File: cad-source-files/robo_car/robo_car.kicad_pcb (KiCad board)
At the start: 2 copper layers, 100 x 100 mm, 87 parts, among them J1 Conn_01x06_MountingPin, J16 Conn_01x02_MountingPin, J2 ftdi_conn, J3 Conn_01x06_MountingPin, J4 Conn_01x04, J5 Conn_01x04, J6 Conn_01x06_MountingPin, J7 Conn_01x02_MountingPin, J8 Conn_01x02_MountingPin, SW1 SW_Push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

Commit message: move Olivia's stuffy stuff to the correct repo
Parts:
- removed D7: D_TVS_x2_AAC, Package_TO_SOT_SMD:SOT-23
- removed U5: Trans_CAN_SN65HVD230DR, Package_SO:CAN-TRANS-SN65HVD230DR
- added C14: 22uF, Capacitor_SMD:C_0805_2012Metric, F.Cu at (175.7, 147.5)
- added C16: 22uF, Capacitor_SMD:C_0805_2012Metric, F.Cu at (179.4, 126.5)
- added H28: MountingHole, MountingHole:MountingHole_3.2mm_M3_ISO14580, F.Cu at (190.0, 111.0)
- added H29: MountingHole, MountingHole:MountingHole_3.2mm_M3_ISO14580, F.Cu at (110.0, 111.0)
- J2: footprint Connector_JST:JST_SH_BM06B-SRSS-TB_1x06-1MP_P1.00mm_Vertical -> Connector_JST:JST_SH_SM06B-SRSS-TB_1x06-1MP_P1.00mm_Horizontal
- J4: value Conn_01x04 -> Barrel_Jack; footprint Connector_JST:JST_PH_B4B-PH-SM4-TB_1x04-1MP_P2.00mm_Vertical -> Connector_BarrelJack:BarrelJack_Horizontal
- J5: footprint Connector_JST:JST_PH_S4B-PH-SM4-TB_1x04-1MP_P2.00mm_Horizontal -> Connector_PinSocket_2.54mm:PinSocket_1x04_P2.54mm_Vertical
- moved C9 45.6 mm to (181.6, 141.7), turned to 180 degrees
- moved C15 41.3 mm to (179.5, 123.7), turned to 0 degrees
- moved J5 14.8 mm to (146.9, 144.7), turned to -90 degrees
- moved J2 13.2 mm to (129.6, 146.7), turned to 0 degrees
- moved J4 6.18 mm to (118.4, 136.2)
- moved R3 4.47 mm to (185.7, 110.2)
- moved R6 3.52 mm to (181.7, 143.8)
- moved C7 3.49 mm to (178.0, 144.7), turned to 90 degrees
- moved U2 1.50 mm to (180.8, 135.9)
- moved H14 1.00 mm to (110.0, 146.0)
- moved H19 1.00 mm to (190.0, 146.0)
- moved H21 1.00 mm to (110.0, 120.0)
- moved H22 1.00 mm to (190.0, 120.0)
- moved H23 1.00 mm to (190.0, 138.0)
- moved H24 1.00 mm to (110.0, 138.0)
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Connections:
- C15 pad 1: +3V3 -> /VREG_OUT
- J4 pad 1: /CAN_H -> VBUS
- J4 pad 2: /CAN_L -> GND
- J4 pad 3: VBUS -> (no net)
- J5 pad 1: /CAN_H -> +3V3
- J5 pad 2: /CAN_L -> GND
- J5 pad 3: VBUS -> /LCD_SCL
- J5 pad 4: GND -> /LCD_SDA
- U3 pad 26: /CAN_TX -> /INPUT_C
- U3 pad 27: /CAN_RX -> /INPUT_A
- U3 pad 28: /INPUT_C -> /INPUT_B
- U3 pad 29: /INPUT_A -> /SERVO_1
- U3 pad 30: /INPUT_B -> /SERVO_0
- U3 pad 31: /SERVO_1 -> /SCL
- U3 pad 33: /SERVO_0 -> /SDA
- U3 pad 36: /SCL -> /LCD_SCL
- U3 pad 37: /SDA -> /LCD_SDA
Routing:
- net /CAN_L: track 38.1 -> 0.00 mm
- net /CAN_SLP: track 33.4 -> 0.00 mm, vias 4 -> 0
- net +3V3: track 268.6 -> 242.6 mm, vias 6 -> 4
- net /CAN_RX: track 25.3 -> 0.00 mm, vias 2 -> 0
- net /RESET: track 40.3 -> 62.5 mm
- net /CAN_H: track 21.9 -> 0.00 mm
- net /TXDO: track 8.71 -> 27.7 mm, vias 2 -> 0
- net /RXD0: track 8.82 -> 26.2 mm, vias 2 -> 0
- net /CAN_TX: track 17.4 -> 0.00 mm, vias 2 -> 0
- net /LCD_SDA: track 0.00 -> 14.8 mm
- net /LCD_SCL: track 0.00 -> 12.2 mm
- net /SCL: track 82.8 -> 76.5 mm
- net /BOOT: track 23.2 -> 28.7 mm
- net VBUS: track 78.2 -> 83.0 mm, vias 20 -> 2
- net /SDA: track 84.0 -> 79.4 mm
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- removed copper zone on B.Cu, net VBUS
- removed copper zone on F.Cu, net VBUS
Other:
- board text added: "14"
- board text removed: "22"
- board text removed: "23"
- board text removed: "RX 16"
- board text removed: "TX 4"

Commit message: add logo
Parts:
- added G***: LOGO, Symbol:mechanical_mustache_25mm_painted, F.Cu at (138.3, 133.2)

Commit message: Still gotta fix the Angie zong shtuff but thats mostly it
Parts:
- removed the G*** at (138.3, 133.2)
- added G***: LOGO, Symbol:Mustache20mm, F.Cu at (135.9, 132.9)
- added REF**: Polarity_Center_Positive_6mm_SilkScreen, Symbol:Polarity_Center_Positive_6mm_SilkScreen, B.Cu at (125.9, 146.8)
- moved D3 4.64 mm to (182.9, 103.1)
- moved R5 3.66 mm to (182.1, 100.1), turned to 0 degrees
- moved R3 2.36 mm to (183.7, 109.0), turned to 90 degrees
- moved SW1 1.57 mm to (186.4, 103.0)
- moved C10 1.53 mm to (180.1, 103.6)
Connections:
- J2 pad 5: VBUS -> unconnected-(J2-Pad5)
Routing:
- net VBUS: track 83.0 -> 64.3 mm
- net +3V3: track 242.6 -> 236.3 mm, vias 4 -> 6
- net /HBT_LED: track 35.9 -> 39.8 mm
- net /FUNCTION_BUTTON: track 50.9 -> 49.9 mm, vias 0 -> 2
- net Net-(D3-Pad1): track 2.88 -> 2.29 mm
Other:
- board text added: "22"
- board text added: "23"
- board text added: "Lefty"
- board text added: "Mo the Mustached Robot Car"
- board text added: "Righty"
- board text added: "Version 1_3"
- board text added: "github.com/Mechanical-Mustaches/mini_mustache"
- board text added: "port_a"
- board text added: "port_b"
- board text added: "port_c"
- board text added: "taftrobotics8122.wixsite.com/mechanical-mustaches"
- board text removed: "Louie"
- board text removed: "Roger"

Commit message: squiggly squiggly
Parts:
- removed the G*** at (150.8, 101.3)
- added G***: LOGO, Symbol:Squiggly, F.Cu at (150.3, 98.4)
- added G***: LOGO, Symbol:Smiley, F.Cu at (150.6, 104.0)
- added G***: LOGO, Symbol:MustacheSS, F.Cu at (150.9, 100.9)
- added G***: LOGO, Symbol:stache_station, F.Cu at (152.4, 102.3)
- moved G*** 1.69 mm to (136.8, 131.5)

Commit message: ok NOW its done
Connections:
- net /ANALOG_A renamed /IO39
- net /ANALOG_B renamed /IO34
- net /ANALOG_C renamed /IO35
- net /ANALOG_D renamed /IO32
- net /INPUT_A renamed /IO16
- net /INPUT_B renamed /IO17
- net /INPUT_C renamed /IO4
- net /INPUT_D renamed /IO13
- net /SCL renamed /IO19
- net /SDA renamed /IO21
- net /SERVO_0 renamed /IO18
- net /SERVO_1 renamed /IO5
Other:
- board text added: "16"

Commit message: gettin down with the qwiic-ness
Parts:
- added J9: Conn_01x02_MountingPin, Connector_JST:JST_XH_2_VERTICAL, F.Cu at (77.0, 132.0)
- added SW3: SW_SPDT, Button_Switch_THT:SW_SLIDE_SS-12D10L9, F.Cu at (64.1, 128.0)
- moved H12 5.00 mm to (105.0, 75.0)
- moved H13 5.00 mm to (105.0, 65.0)
- moved H15 5.00 mm to (195.0, 95.0)
- moved H17 5.00 mm to (105.0, 95.0)
- moved H18 5.00 mm to (195.0, 75.0)
- moved H20 5.00 mm to (195.0, 85.0)
- moved H25 5.00 mm to (195.0, 65.0)
- moved H5 5.00 mm to (105.0, 85.0)
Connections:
- U3 pad 24: /CAN_SLP -> unconnected-(U3-Pad24)
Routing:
- net GND: vias 393 -> 385
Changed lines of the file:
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@@
   (net 34 "unconnected-(U3-Pad21)")
   (net 35 "unconnected-(U3-Pad22)")
-  (net 36 "/CAN_SLP")
+  (net 36 "unconnected-(J9-Pad1)")
   (net 37 "/IO39")
   (net 38 "Net-(D12-Pad1)")
@@
   (net 55 "/IO19")
   (net 56 "/IO21")
+  (net 57 "unconnected-(J9-Pad2)")
+  (net 58 "unconnected-(J9-PadMP)")
+  (net 59 "unconnected-(SW3-Pad1)")
+  (net 60 "unconnected-(SW3-Pad2)")
+  (net 61 "unconnected-(SW3-Pad3)")
+  (net 62 "unconnected-(U3-Pad24)")
   (footprint "MountingHole:MountingHole_3.2mm_M3_ISO14580" (layer "F.Cu")
     (at 110 146)
@@
   )
   (footprint "MountingHole:MountingHole_3.2mm_M3_ISO14580" (layer "F.Cu")
-    (at 195 70)
+    (at 195 65)
     (descr "Mounting Hole 3.2mm, no annular, M3, ISO14580")
     (tags "mounting hole 3.2mm no annular m3 iso14580")
@@
   )
   (footprint "MountingHole:MountingHole_3.2mm_M3_ISO14580" (layer "F.Cu")
-    (at 105 100)
+    (at 105 95)
     (descr "Mounting Hole 3.2mm, no annular, M3, ISO14580")
     (tags "mounting hole 3.2mm no annular m3 iso14580")
@@
   )
   (footprint "MountingHole:MountingHole_3.2mm_M3_ISO14580" (layer "F.Cu")
-    (at 195 80)
+    (at 195 75)
     (descr "Mounting Hole 3.2mm, no annular, M3, ISO14580")
     (tags "mounting hole 3.2mm no annular m3 iso14580")
@@
       (net 14 "/NEO_BAR") (pinfunction "NOISE@BOOT-A2-IO15") (pintype "bidirectional"))
     (pad "24" smd rect (at 5.715 9.255 270) (size 2 0.9) (layers "F.Cu" "F.Paste" "F.Mask")
-      (net 36 "/CAN_SLP") (pinfunction "LOW@BOOT-A2-IO2") (pintype "bidirectional"))
+      (net 62 "unconnected-(U3-Pad24)") (pinfunction "LOW@BOOT-A2-IO2") (pintype "bidirectional"))
     (pad "25" smd rect (at 8.5 8.255 180) (size 2 0.9) (layers "F.Cu" "F.Paste" "F.Mask")
       (net 19 "/BOOT") (pinfunction "BOOT-A2-IO0") (pintype "bidirectional"))
@@
     )
   )
+  (footprint "Connector_JST:JST_XH_2_VERTICAL" (layer "F.Cu")
+    (at 77 132)
+    (property "Sheetfile" "robo_car.kicad_sch")
+    (property "Sheetname" "")
+    (attr through_hole)
+    (fp_text reference "J9" (at 0.76 -0.7) (layer "F.Fab")
+      (effects (font (size 1 1) (thickness 0.15)))
+    )
+    (fp_text value "Conn_01x02_MountingPin" (at 0.12 11.12) (layer "F.Fab")
+      (effects (font (size 1 1) (thickness 0.15)))
+    )
+    (fp_line (start 4.75 2) (end -4.25 2) (layer "F.CrtYd") (width 0.12))
+    (fp_line (start 4.75 2) (end 4.75 -5) (layer "F.CrtYd") (width 0.12))
+    (fp_line (start -4.25 -5) (end 4.75 -5) (layer "F.CrtYd") (width 0.12))
+    (fp_line (start -4.25 2) (end -4.25 -5) (layer "F.CrtYd") (width 0.12))
+    (pad "1" smd roundrect (at 1.25 -5.25) (size 1.3 4.5) (layers "F.Cu" "F.Paste" "F.Mask") (roundrect_rratio 0.1)
+      (net 36 "unconnected-(J9-Pad1)") (pinfunction "Pin_1") (pintype "passive"))
+    (pad "2" smd roundrect (at -1.25 -5.25) (size 1.3 4.5) (layers "F.Cu" "F.Paste" "F.Mask") (roundrect_rratio 0.1)
+      (net 57 "unconnected-(J9-Pad2)") (pinfunction "Pin_2") (pintype "passive"))
+    (pad "MP" smd roundrect (at -4.45 -1.75) (size 1.8 3.9) (layers "F.Cu" "F.Paste" "F.Mask") (roundrect_rratio 0.1)
+      (net 58 "unconnected-(J9-PadMP)") (pinfunction "MountPin") (pintype "passive"))
+    (pad "MP" smd roundrect (at 4.45 -1.75) (size 1.8 3.9) (layers "F.Cu" "F.Paste" "F.Mask") (roundrect_rratio 0.1)
+      (net 58 "unconnected-(J9-PadMP)") (pinfunction "MountPin") (pintype "passive"))
+  )
   (footprint "Connector_FFC-FPC:TE_84952-6_1x06-1MP_P1.0mm_Horizontal" (layer "F.Cu")
     (at 150.51 66 180)
@@
   )
   (footprint "MountingHole:MountingHole_3.2mm_M3_ISO14580" (layer "F.Cu")
-    (at 195 90)
+    (at 195 85)
     (descr "Mounting Hole 3.2mm, no annular, M3, ISO14580")
     (tags "mounting hole 3.2mm no annular m3 iso14580")
@@
   )
   (footprint "MountingHole:MountingHole_3.2mm_M3_ISO14580" (layer "F.Cu")
-    (at 105 90)
+    (at 105 85)
     (descr "Mounting Hole 3.2mm, no annular, M3, ISO14580")
     (tags "mounting hole 3.2mm no annular m3 iso14580")
@@
     )
   )
+  (footprint "Button_Switch_THT:SW_SLIDE_SS-12D10L9" (layer "F.Cu")
+    (at 64.09 127.96)
+    (property "Sheetfile" "robo_car.kicad_sch")
+    (property "Sheetname" "")
+    (attr through_hole)
+    (fp_text reference "SW3" (at 0.34 -7.35 unlocked) (layer "F.SilkS") hide
+      (effects (font (size 1 1) (thickness 0.15)))
+    )
+    (fp_text value "SW_SPDT" (at 0.1 2.85 unlocked) (layer "F.Fab")
+      (effects (font (size 0.5 0.5) (thickness 0.1)))
+    )
+    (fp_text user "${REFERENCE}" (at -0.1 -2.4 unlocked) (layer "F.Fab")
+      (effects (font (size 1 1) (thickness 0.15)))
+    )
+    (fp_line (start 6.5 -3.4) (end -6.5 -3.4) (layer "F.SilkS") (width 0.12))
+    (fp_line (start 6.5 3.4) (end 6.5 -3.4) (layer "F.SilkS") (width 0.12))
+    (fp_line (start -6.5 -3.4) (end -6.5 3.4) (layer "F.SilkS") (width 0.12))
+    (fp_line (start -6.5 3.4) (end 6.5 3.4) (layer "F.SilkS") (width 0.12))
+    (pad "1" thru_hole circle (at -4.7 0) (size 2.4 2.4) (drill 1.4) (layers *.Cu *.Mask)
+      (net 59 "unconnected-(SW3-Pad1)") (pinfunction "A") (pintype "passive"))
+    (pad "2" thru_hole circle (at 0 0) (size 2.4 2.4) (drill 1.4) (layers *.Cu *.Mask)
+      (net 60 "unconnected-(SW3-Pad2)") (pinfunction "B") (pintype "passive"))
+    (pad "3" thru_hole circle (at 4.7 0) (size 2.4 2.4) (drill 1.4) (layers *.Cu *.Mask)
+      (net 61 "unconnected-(SW3-Pad3)") (pinfunction "C") (pintype "passive"))
+  )
   (footprint "Capacitor_SMD:C_0603_1608Metric" (layer "F.Cu")
     (at 151.004648 79.914648 -90)
@@
   )
   (footprint "MountingHole:MountingHole_3.2mm_M3_ISO14580" (layer "F.Cu")
-    (at 105 70)
+    (at 105 65)
     (descr "Mounting Hole 3.2mm, no annular, M3, ISO14580")
     (tags "mounting hole 3.2mm no annular m3 iso14580")
@@
   )
   (footprint "MountingHole:MountingHole_3.2mm_M3_ISO14580" (layer "F.Cu")
-    (at 105 80)
+    (at 105 75)
     (descr "Mounting Hole 3.2mm, no annular, M3, ISO14580")
     (tags "mounting hole 3.2mm no annular m3 iso14580")
@@
   )
   (footprint "MountingHole:MountingHole_3.2mm_M3_ISO14580" (layer "F.Cu")
-    (at 195 100)
+    (at 195 95)
     (descr "Mounting Hole 3.2mm, no annular, M3, ISO14580")
     (tags "mounting hole 3.2mm no annular m3 iso14580")
@@
   (via (at 159.004 106.426) (size 0.8) (drill 0.4) (layers "F.Cu" "B.Cu") (free) (net 2))
   (via (at 165.1 113.03) (size 0.8) (drill 0.4) (layers "F.Cu" "B.Cu") (free) (net 2))
-  (via (at 105 95) (size 0.8) (drill 0.4) (layers "F.Cu" "B.Cu") (free) (net 2))
   (via (at 145.288 113.538) (size 0.8) (drill 0.4) (layers "F.Cu" "B.Cu") (free) (net 2))
   (via (at 120.65 71.628) (size 0.8) (drill 0.4) (layers "F.Cu" "B.Cu") (free) (net 2))
@@
   (via (at 172.974 128.778) (size 0.8) (drill 0.4) (layers "F.Cu" "B.Cu") (free) (net 2))
   (via (at 122.936 87.122) (size 0.8) (drill 0.4) (layers "F.Cu" "B.Cu") (free) (net 2))
-  (via (at 195 85) (size 0.8) (drill 0.4) (layers "F.Cu" "B.Cu") (free) (net 2))
   (via (at 166.624 79.248) (size 0.8) (drill 0.4) (layers "F.Cu" "B.Cu") (free) (net 2))
   (via (at 120.396 75.184) (size 0.8) (drill 0.4) (layers "F.Cu" "B.Cu") (free) (net 2))
@@
   (via (at 110 85) (size 0.8) (drill 0.4) (layers "F.Cu" "B.Cu") (free) (net 2))
   (via (at 123.444 123.19) (size 0.8) (drill 0.4) (layers "F.Cu" "B.Cu") (free) (net 2))
-  (via (at 105 65) (size 0.8) (drill 0.4) (layers "F.Cu" "B.Cu") (free) (net 2))
   (via (at 156.718 126.492) (size 0.8) (drill 0.4) (layers "F.Cu" "B.Cu") (free) (net 2))
   (via (at 187.452 91.186) (size 0.8) (drill 0.4) (layers "F.Cu" "B.Cu") (free) (net 2))
@@
   (via (at 150.368 118.872) (size 0.8) (drill 0.4) (layers "F.Cu" "B.Cu") (free) (net 2))
   (via (at 157.226 77.47) (size 0.8) (drill 0.4) (layers "F.Cu" "B.Cu") (free) (net 2))
-  (via (at 195 95) (size 0.8) (drill 0.4) (layers "F.Cu" "B.Cu") (free) (net 2))
   (via (at 107.188 125.222) (size 0.8) (drill 0.4) (layers "F.Cu" "B.Cu") (free) (net 2))
   (via (at 128.016 71.628) (size 0.8) (drill 0.4) (layers "F.Cu" "B.Cu") (free) (net 2))
@@
   (via (at 137.668 99.314) (size 0.8) (drill 0.4) (layers "F.Cu" "B.Cu") (free) (net 2))
   (via (at 169.418 118.872) (size 0.8) (drill 0.4) (layers "F.Cu" "B.Cu") (free) (net 2))
-  (via (at 195 75) (size 0.8) (drill 0.4) (layers "F.Cu" "B.Cu") (free) (net 2))
   (via (at 185.21 133.19) (size 0.8) (drill 0.4) (layers "F.Cu" "B.Cu") (free) (net 2))
   (via (at 132.842 96.52) (size 0.8) (drill 0.4) (layers "F.Cu" "B.Cu") (free) (net 2))
@@
   (via (at 156.21 61.214) (size 0.8) (drill 0.4) (layers "F.Cu" "B.Cu") (free) (net 2))
   (via (at 181.102 74.422) (size 0.8) (drill 0.4) (layers "F.Cu" "B.Cu") (free) (net 2))
-  (via (at 105 75) (size 0.8) (drill 0.4) (layers "F.Cu" "B.Cu") (free) (net 2))
   (via (at 124.714 92.964) (size 0.8) (drill 0.4) (layers "F.Cu" "B.Cu") (free) (net 2))
   (via (at 165 92.5) (size 0.8) (drill 0.4) (layers "F.Cu" "B.Cu") (free) (net 2))
-  (via (at 195 65) (size 0.8) (drill 0.4) (layers "F.Cu" "B.Cu") (free) (net 2))
   (via (at 114.554 94.234) (size 0.8) (drill 0.4) (layers "F.Cu" "B.Cu") (free) (net 2))
   (via (at 137.668 112.268) (size 0.8) (drill 0.4) (layers "F.Cu" "B.Cu") (free) (net 2))
@@
   (via (at 188.54 98.45) (size 0.8) (drill 0.4) (layers "F.Cu" "B.Cu") (free) (net 2))
   (via (at 172.72 85.852) (size 0.8) (drill 0.4) (layers "F.Cu" "B.Cu") (free) (net 2))
-  (via (at 105 85) (size 0.8) (drill 0.4) (layers "F.Cu" "B.Cu") (free) (net 2))
   (via (at 130 82.5) (size 0.8) (drill 0.4) (layers "F.Cu" "B.Cu") (free) (net 2))
   (via (at 152.5 102.5) (size 0.8) (drill 0.4) (layers "F.Cu" "B.Cu") (free) (net 2))

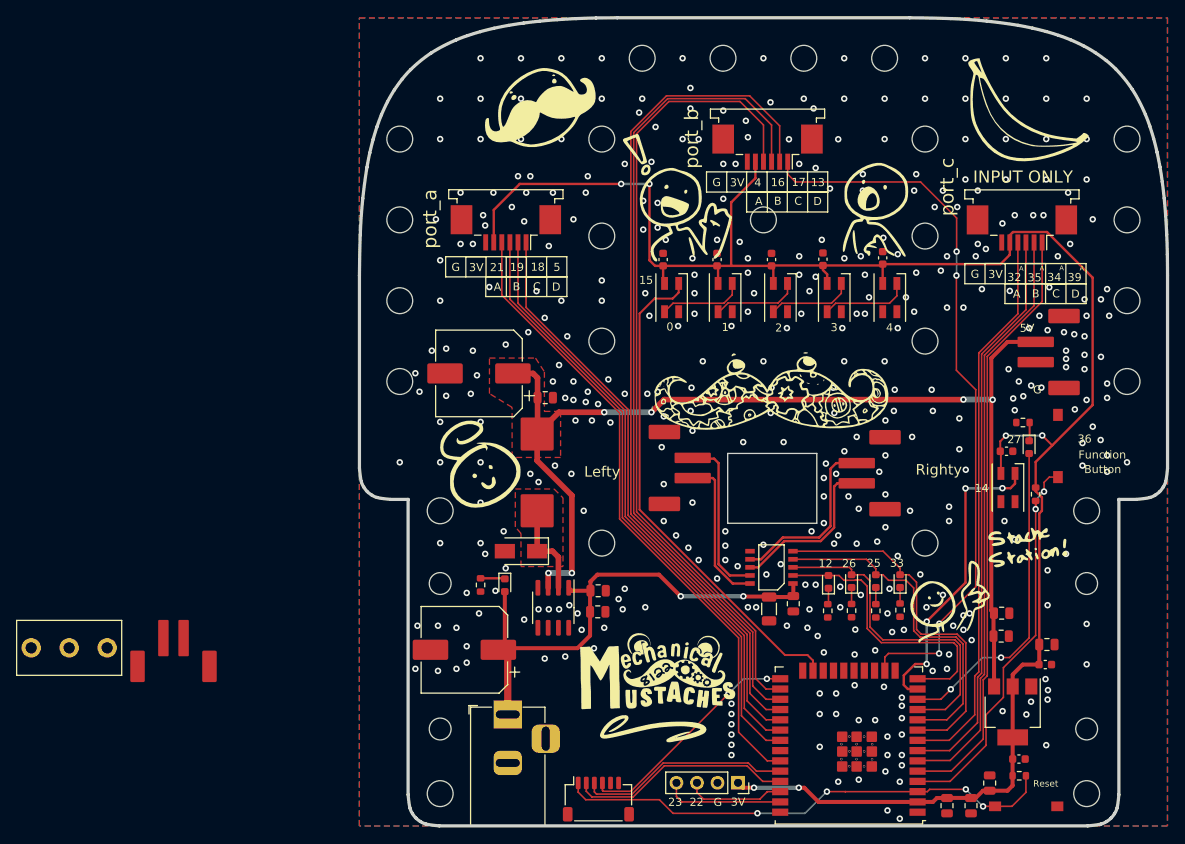
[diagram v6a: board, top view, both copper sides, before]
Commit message: mo 4 has spawned
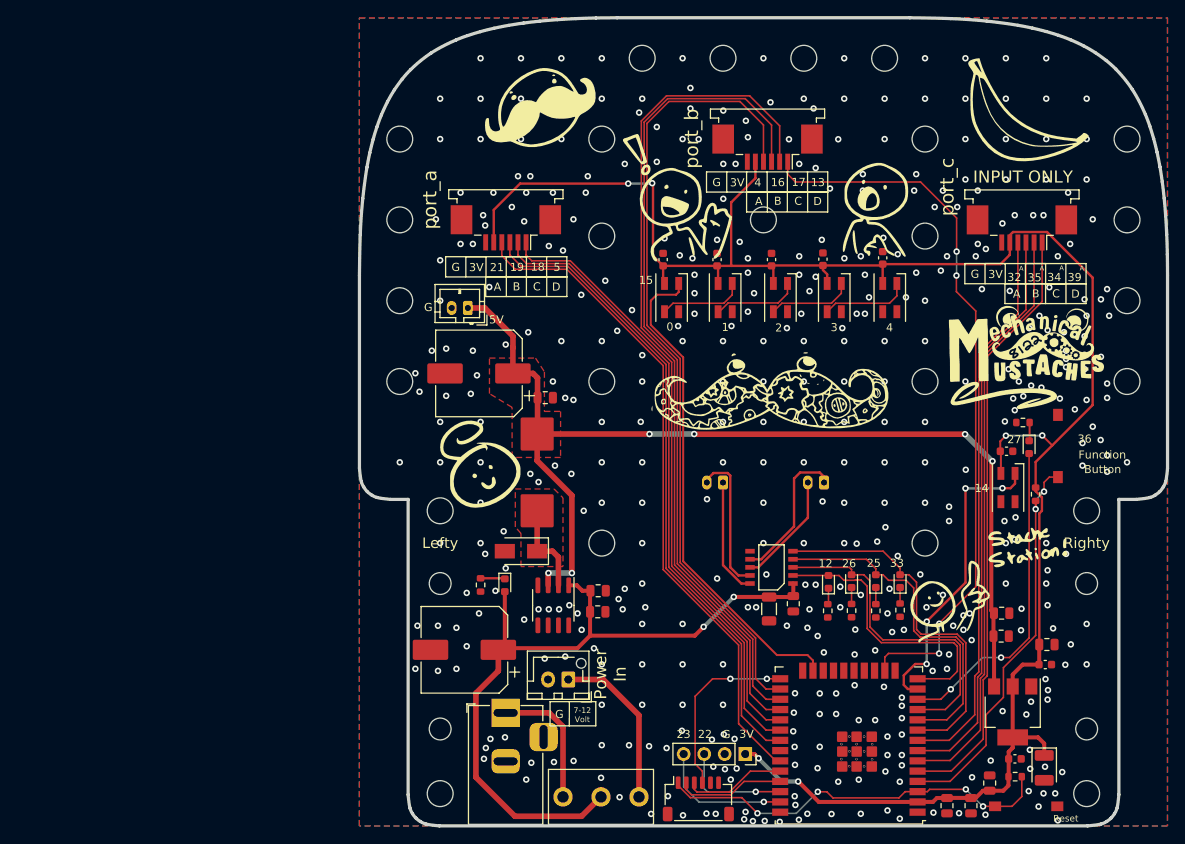
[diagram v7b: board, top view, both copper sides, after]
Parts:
- added C19: 100uF, Capacitor_Tantalum_SMD:CP_EIA-3528-21_Kemet-B, F.Cu at (184.8, 142.8)
- J16, J8: footprint Connector_JST:JST_XH_2_VERTICAL -> Connector_JST:JST_PH_S2B-PH-K_1x02_P2.00mm_Horizontal; moved to B.Cu
- J7: footprint Connector_JST:JST_XH_2_VERTICAL -> Connector_JST:JST_PH_B2B-PH-K_1x02_P2.00mm_Vertical
- J9: footprint Connector_JST:JST_XH_2_VERTICAL -> Connector_JST:JST_XH_B2B-XH-AM_1x02_P2.50mm_Vertical
- moved J7 75.7 mm to (113.4, 85.9), turned to 180 degrees
- moved SW3 68.3 mm to (129.9, 146.4), turned to 180 degrees
- moved G*** 61.0 mm to (182.5, 91.0)
- moved G*** 59.9 mm to (193.7, 57.2)
- moved J9 48.9 mm to (125.8, 131.9), turned to 180 degrees
- moved J2 12.4 mm to (141.9, 146.7)
- moved J16 9.37 mm to (157.5, 107.5), turned to 180 degrees
- moved J8 9.18 mm to (145.0, 107.5), turned to 180 degrees
- moved H7 5.00 mm to (130.0, 95.0)
- moved H9 5.00 mm to (170.0, 95.0)
- moved J5 3.67 mm to (147.8, 141.1)
- moved R6 0.52 mm to (181.2, 143.9)
- moved C9 0.50 mm to (181.1, 141.7)
- moved J4 0.33 mm to (118.1, 136.0)
- moved U1 0.30 mm to (124.0, 122.7)
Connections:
- J4 pad 1: VBUS -> Net-(J4-Pad1)
- J9 pad 1: unconnected-(J9-Pad1) -> Net-(SW3-Pad1)
- J9 pad 2: unconnected-(J9-Pad2) -> GND
- SW3 pad 1: unconnected-(SW3-Pad1) -> Net-(SW3-Pad1)
- SW3 pad 2: unconnected-(SW3-Pad2) -> VBUS
- SW3 pad 3: unconnected-(SW3-Pad3) -> Net-(J4-Pad1)
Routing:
- net VBUS: track 64.3 -> 91.8 mm
- net Net-(SW3-Pad1): track 0.00 -> 20.7 mm
- net Net-(J4-Pad1): track 0.00 -> 16.5 mm
- net /TXDO: track 27.7 -> 13.4 mm
- net /RXD0: track 26.2 -> 12.7 mm
- net /RESET: track 62.5 -> 50.0 mm
- net /VREG_OUT: track 139.4 -> 131.2 mm
- net Net-(J16-Pad2): track 20.5 -> 14.1 mm
- net /BOOT: track 28.7 -> 22.5 mm
- net +3V3: track 236.3 -> 242.0 mm
- net Net-(J16-Pad1): track 22.3 -> 18.0 mm
- net Net-(J8-Pad1): track 18.7 -> 14.5 mm
- net /IO19: track 76.5 -> 79.9 mm
- net /IO21: track 79.4 -> 82.5 mm
- net /IO18: track 74.8 -> 77.9 mm
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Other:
- outline, holes or cut-outs redrawn
- board text added: "7-12 Volt"
- board text added: "Power In"
- board text added: "Version 1_4"
- board text removed: "Version 1_3"

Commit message: 12-2 boards ordered
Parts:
- added D2: SX35_SCHOTTKY, Diode_SMD:D_SMA, F.Cu at (131.7, 138.7)
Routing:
- net VBUS: track 91.8 -> 98.2 mm
- net Net-(J9-Pad1): track 20.7 -> 21.9 mm
